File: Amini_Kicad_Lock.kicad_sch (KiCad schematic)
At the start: 40 parts, among them J1 Conn_01x02_Pin, J2 Conn_01x04, J3 MM8130-2600RA2, J4 Conn_01x03_Pin, U1 nRF5340-QKxx, X1 ${ALTIUM_VALUE}, X2 ${ALTIUM_VALUE}

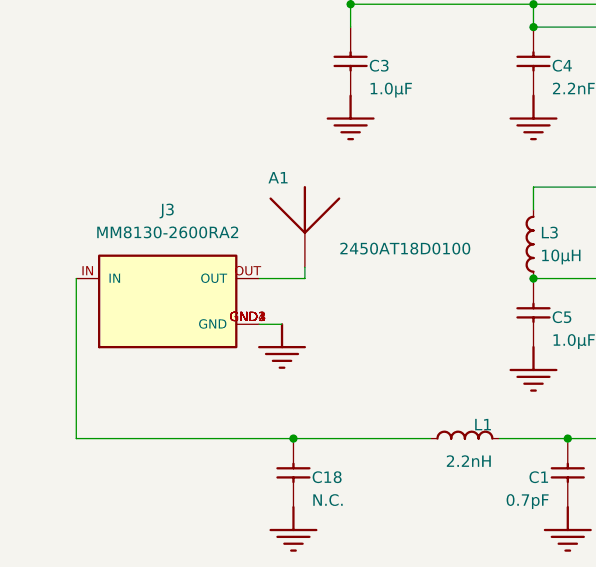
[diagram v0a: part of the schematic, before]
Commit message: New antenna design done
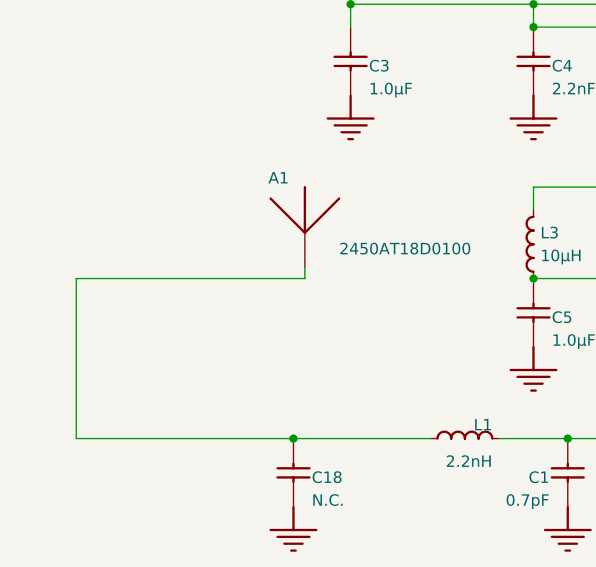
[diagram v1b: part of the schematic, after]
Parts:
- removed J3: MM8130-2600RA2, MM8130-2600RA2 antenna:MURATA_MM8130-2600RA2, symbol MM8130-2600RA2:MM8130-2600RA2
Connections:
- net at C18.2, L1.2: now also A1.1
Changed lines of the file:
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@@
 	(wire
 		(pts
+			(xy 20.32 115.57) (xy 45.72 115.57)
+		)
+		(stroke
+			(width 0)
+			(type default)
+		)
+	)
+	(wire
+		(pts
 			(xy 203.2 15.24) (xy 213.36 15.24)
 		)
@@
 	(wire
 		(pts
-			(xy 45.72 115.57) (xy 40.64 115.57)
-		)
-		(stroke
-			(width 0)
-			(type default)
-		)
-	)
-	(wire
-		(pts
 			(xy 234.95 119.38) (xy 259.08 119.38)
 		)
@@
 	(wire
 		(pts
-			(xy 43.18 120.65) (xy 40.64 120.65)
-		)
-		(stroke
-			(width 0)
-			(type default)
-		)
-	)
-	(wire
-		(pts
 			(xy 20.32 133.35) (xy 20.32 115.57)
 		)
@@
 	)
 	(symbol
-		(lib_id "MM8130-2600RA2:MM8130-2600RA2")
-		(at 30.48 118.11 0)
-		(unit 1)
-		(exclude_from_sim no)
-		(in_bom yes)
-		(on_board yes)
-		(dnp no)
-		(fields_autoplaced yes)
-		(property "Reference" "J3"
-			(at 30.48 107.95 0)
-			(effects
-				(font
-					(size 1.27 1.27)
-				)
-			)
-		)
-		(property "Value" "MM8130-2600RA2"
-			(at 30.48 110.49 0)
-			(effects
-				(font
-					(size 1.27 1.27)
-				)
-			)
-		)
-		(property "Footprint" "MM8130-2600RA2 antenna:MURATA_MM8130-2600RA2"
-			(at 30.48 118.11 0)
-			(effects
-				(font
-					(size 1.27 1.27)
-				)
-				(justify bottom)
-				(hide yes)
-			)
-		)
-		(property "Datasheet" ""
-			(at 30.48 118.11 0)
-			(effects
-				(font
-					(size 1.27 1.27)
-				)
-				(hide yes)
-			)
-		)
-		(property "Description" ""
-			(at 30.48 118.11 0)
-			(effects
-				(font
-					(size 1.27 1.27)
-				)
-				(hide yes)
-			)
-		)
-		(property "MF" "Murata"
-			(at 30.48 118.11 0)
-			(effects
-				(font
-					(size 1.27 1.27)
-				)
-				(justify bottom)
-				(hide yes)
-			)
-		)
-		(property "Description_1" "\nSWF Connector Receptacle, Female Socket 50 Ohms Surface Mount Solder\n"
-			(at 30.48 118.11 0)
-			(effects
-				(font
-					(size 1.27 1.27)
-				)
-				(justify bottom)
-				(hide yes)
-			)
-		)
-		(property "Package" "None"
-			(at 30.48 118.11 0)
-			(effects
-				(font
-					(size 1.27 1.27)
-				)
-				(justify bottom)
-				(hide yes)
-			)
-		)
-		(property "Price" "None"
-			(at 30.48 118.11 0)
-			(effects
-				(font
-					(size 1.27 1.27)
-				)
-				(justify bottom)
-				(hide yes)
-			)
-		)
-		(property "Check_prices" "https://www.snapeda.com/parts/MM8130-2600RA2/Murata+Electronics+North+America/view-part/?ref=eda"
-			(at 30.48 118.11 0)
-			(effects
-				(font
-					(size 1.27 1.27)
-				)
-				(justify bottom)
-				(hide yes)
-			)
-		)
-		(property "SnapEDA_Link" "https://www.snapeda.com/parts/MM8130-2600RA2/Murata+Electronics+North+America/view-part/?ref=snap"
-			(at 30.48 118.11 0)
-			(effects
-				(font
-					(size 1.27 1.27)
-				)
-				(justify bottom)
-				(hide yes)
-			)
-		)
-		(property "MP" "MM8130-2600RA2"
-			(at 30.48 118.11 0)
-			(effects
-				(font
-					(size 1.27 1.27)
-				)
-				(justify bottom)
-				(hide yes)
-			)
-		)
-		(property "Availability" "In Stock"
-			(at 30.48 118.11 0)
-			(effects
-				(font
-					(size 1.27 1.27)
-				)
-				(justify bottom)
-				(hide yes)
-			)
-		)
-		(property "MANUFACTURER" "MURATA"
-			(at 30.48 118.11 0)
-			(effects
-				(font
-					(size 1.27 1.27)
-				)
-				(justify bottom)
-				(hide yes)
-			)
-		)
-		(pin "GND2"
-		)
-		(pin "GND4"
-		)
-		(pin "OUT"
-		)
-		(pin "GND3"
-		)
-		(pin "IN"
-		)
-		(pin "GND1"
-		)
-		(instances
-			(project "Amini_Kicad_Lock"
-				(path "/030762cc-f5a7-43ca-9be6-07123a61669e"
-					(reference "J3")
-					(unit 1)
-				)
-			)
-		)
-	)
-	(symbol
 		(lib_id "nrf5340_qkaa_config3-altium-import:GND_POWER_GROUND")
 		(at 71.12 163.83 0)
@@
 					(unit 1)
 				)
-			)
-		)
-	)
-	(symbol
-		(lib_id "pca10143_sheet2_nrf5340_mcu-altium-import:GND_POWER_GROUND")
-		(at 43.18 120.65 0)
-		(mirror y)
-		(unit 1)
-		(exclude_from_sim no)
-		(in_bom yes)
-		(on_board yes)
-		(dnp no)
-		(property "Reference" "#PWR05"
-			(at 43.18 120.65 0)
-			(effects
-				(font
-					(size 1.27 1.27)
-				)
-				(hide yes)
-			)
-		)
-		(property "Value" "GND"
-			(at 43.18 127 0)
-			(effects
-				(font
-					(size 1.27 1.27)
-				)
-				(hide yes)
-			)
-		)
-		(property "Footprint" ""
-			(at 43.18 120.65 0)
-			(effects
-				(font
-					(size 1.27 1.27)
-				)
-				(hide yes)
-			)
-		)
-		(property "Datasheet" ""
-			(at 43.18 120.65 0)
-			(effects
-				(font
-					(size 1.27 1.27)
-				)
-				(hide yes)
-			)
-		)
-		(property "Description" ""
-			(at 43.18 120.65 0)
-			(effects
-				(font
-					(size 1.27 1.27)
-				)
-				(hide yes)
-			)
-		)
-		(pin ""
-		)
-		(instances
-			(project "Amini_Kicad_Lock"
-				(path "/030762cc-f5a7-43ca-9be6-07123a61669e"
-					(reference "#PWR05")
-					(unit 1)
-				)

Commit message: some changes done
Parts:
- removed J4: Conn_01x03_Pin, Connector_PinHeader_2.00mm:PinHeader_1x03_P2.00mm_Vertical, symbol Connector:Conn_01x03_Pin
- added C17: 0.7pF, Capacitor_SMD:C_0402_1005Metric_Pad0.74x0.62mm_HandSolder, symbol Device:C
- added C19: ${ALTIUM_VALUE}, Capacitor_SMD:C_0402_1005Metric_Pad0.74x0.62mm_HandSolder, symbol pca10143_sheet2_nrf5340_mcu-altium-import:root_1_CAP
- added J3: Conn_01x04_Pin, Connector_PinHeader_2.00mm:PinHeader_1x04_P2.00mm_Vertical, symbol Connector:Conn_01x04_Pin
- added L4: 2.2nH, Capacitor_SMD:C_0402_1005Metric_Pad0.74x0.62mm_HandSolder, symbol Device:L
- C1, C18, L1: footprint Inductor_SMD:L_0603_1608Metric -> Capacitor_SMD:C_0402_1005Metric_Pad0.74x0.62mm_HandSolder
- J2: footprint Connector_JST:JST_SH_SM04B-SRSS-TB_1x04-1MP_P1.00mm_Horizontal -> Connector_PinHeader_2.54mm:PinHeader_2x02_P2.54mm_Vertical
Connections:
- net GND: now also C17.2, C19.1
- net LED1: now also LED3.1 (C), U1.W1 (NFC1/P0.02), J3.3 (Pin_3); no longer LED1.1 (C), U1.AL29 (AIN5/P0.26)
- net LED2: now also J3.2 (Pin_2)
- net LED3: now also LED1.1 (C), U1.AL29 (AIN5/P0.26), J3.1 (Pin_1); no longer LED3.1 (C), U1.AL9 (IO3/P0.16)
- net at C1.2, L1.1: now also C19.2, L4.1; no longer U1.L31 (ANT)
- net MIC: now reaches U1.AA1 (NFC2/P0.03)
- net MIC: now also J3.4 (Pin_4)
- new net: C17.1, L4.2, U1.L31 (ANT)
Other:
- moved on the sheet: C1, C18, L1
